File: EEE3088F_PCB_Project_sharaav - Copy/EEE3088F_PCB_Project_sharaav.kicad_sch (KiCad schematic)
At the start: 33 parts, among them Q1 NPN, Q2 PNP, Q3 NPN, Q4 PNP, SW1 SW_SPDT_MSM, U1 TPS61200DRC, U2 TPS61200DRC, U3 INA219AxDCN

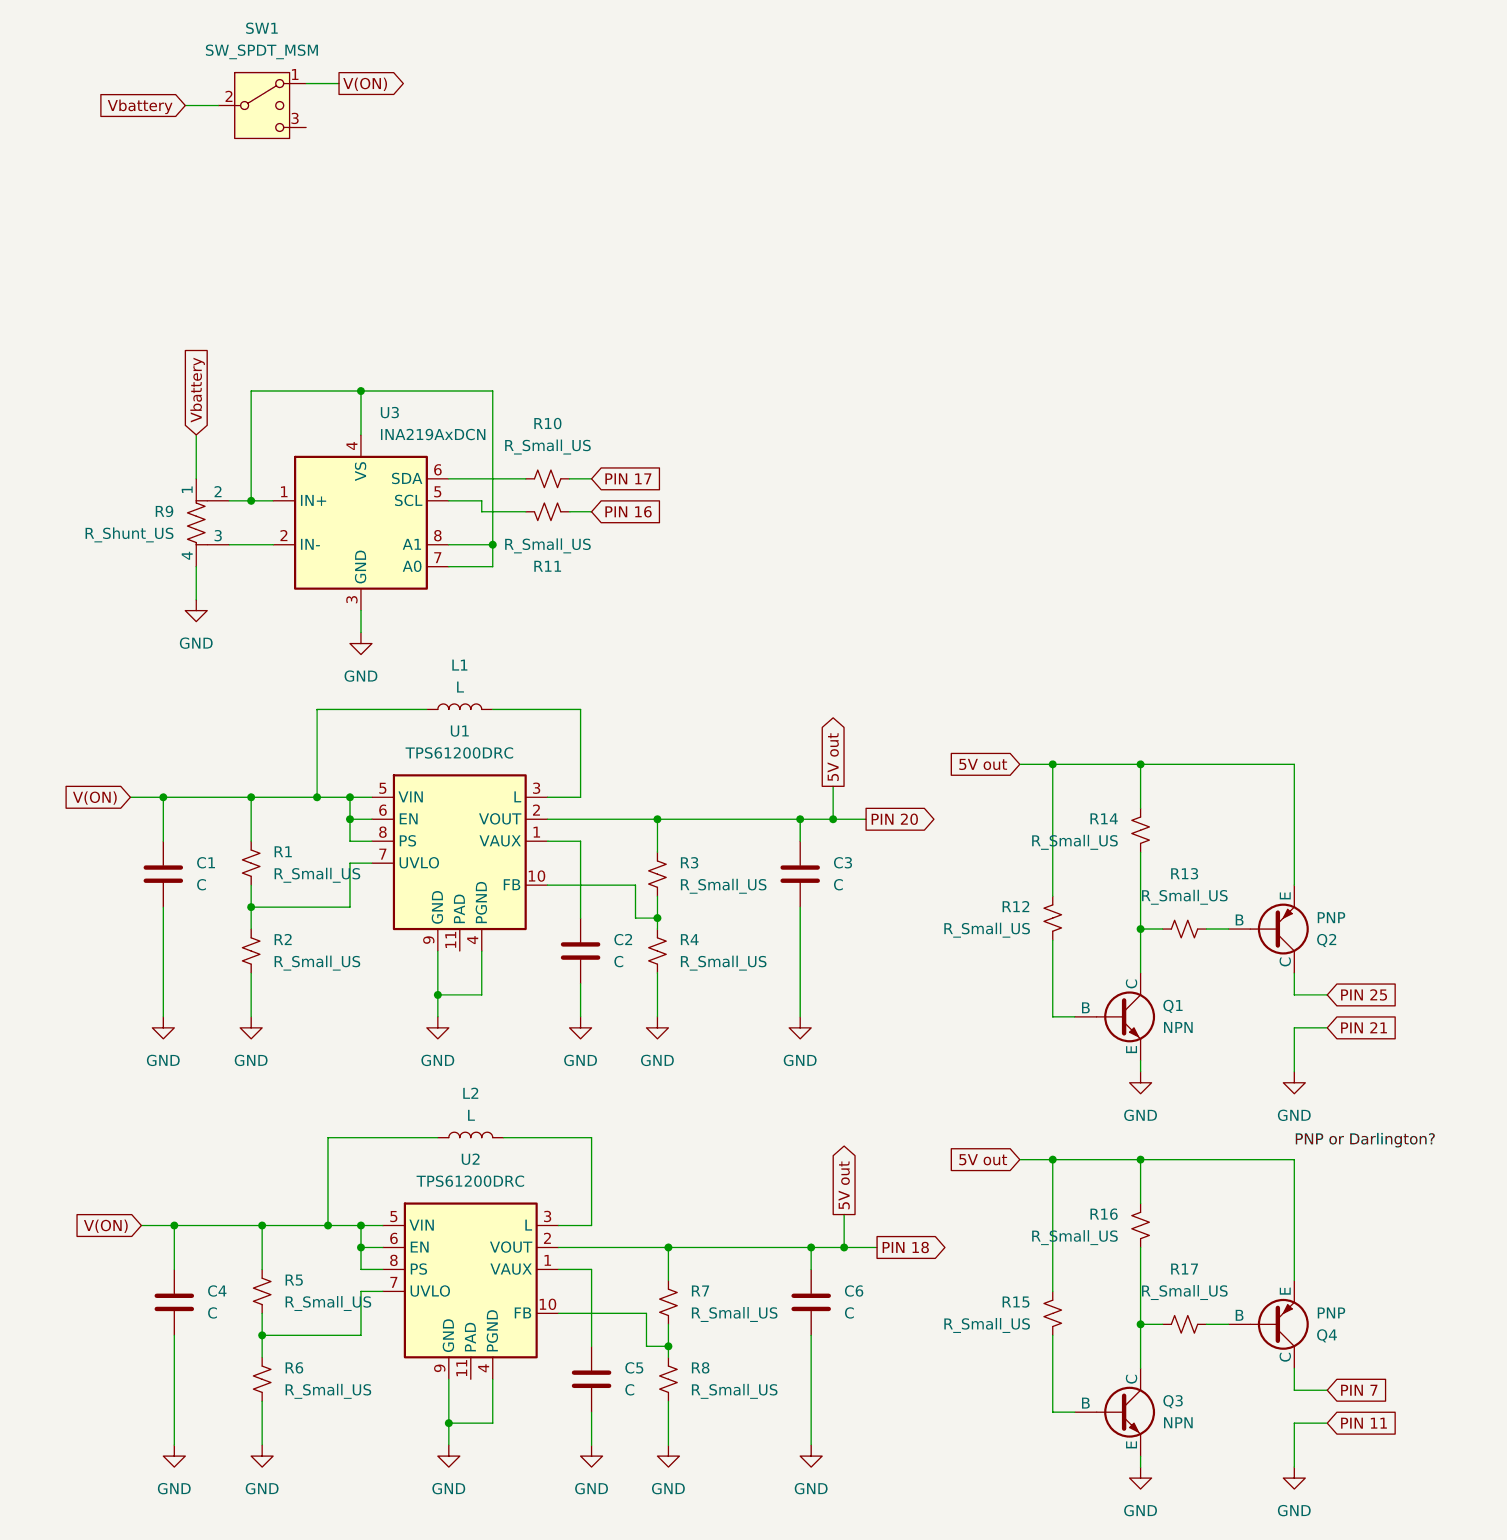
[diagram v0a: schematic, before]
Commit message: Labelled the values for passive components & added the footprints for the ICs and switch.
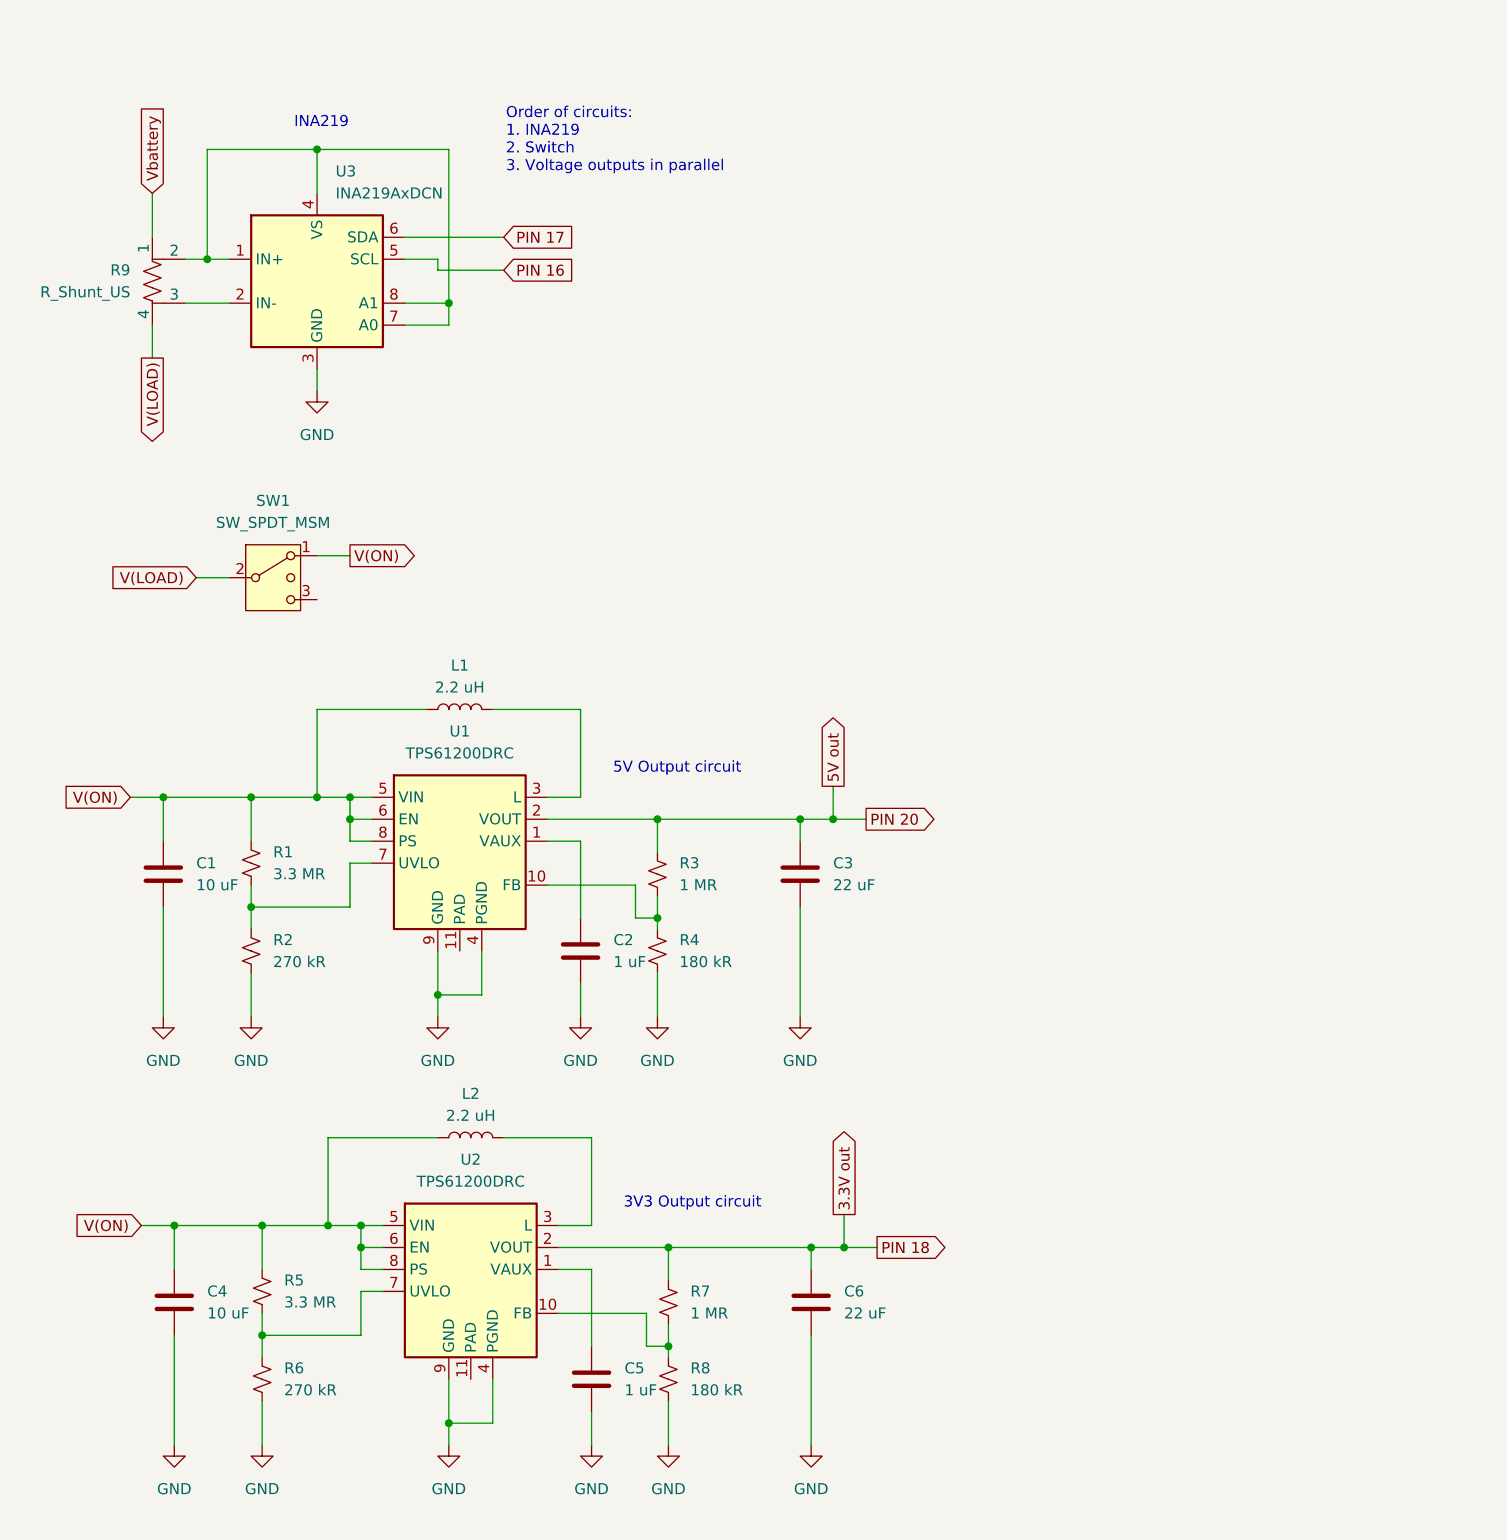
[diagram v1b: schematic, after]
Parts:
- removed Q1, Q3: NPN, symbol Simulation_SPICE:NPN
- removed Q2, Q4: PNP, symbol Simulation_SPICE:PNP
- removed R10, R11, R12, R13, R14, R15, R16, R17: R_Small_US, symbol Device:R_Small_US
- C1, C4: value C -> 10 uF
- C2, C5: value C -> 1 uF
- C3, C6: value C -> 22 uF
- L1, L2: value L -> 2.2 uH
- R1, R5: value R_Small_US -> 3.3 MR
- R2, R6: value R_Small_US -> 270 kR
- R3, R7: value R_Small_US -> 1 MR
- R4, R8: value R_Small_US -> 180 kR
- SW1: footprint (none) -> LIB_SS-12D11G5R:SS12D11G5R
- U1, U2: footprint Package_SON:Texas_S-PVSON-N10_ThermalVias -> LIB_TPS61200DRCR:TPS61200DRCR; JLCPCB Part # (none) -> C140320
- U3: footprint Package_TO_SOT_SMD:SOT-23-8 -> LIB_INA219AIDCNR:SOP65P280X145-8N
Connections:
- net 5V out: no longer C6.1, R7.1, U2.2 (VOUT)
- net GND: no longer R9.4
- net PIN 16: now also U3.5 (SCL)
- net PIN 17: now also U3.6 (SDA)
- net Vbattery: no longer SW1.2 (3)
- new net 3.3V out: C6.1, R7.1, U2.2 (VOUT)
- new net V(LOAD): R9.4, SW1.2 (3)
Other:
- note added: "3V3 Output circuit"
- note added: "5V Output circuit"
- note added: "INA219"
- note added: "Order of circuits: 1. INA219 2. Switch 3. Voltage outputs in parallel"
- moved on the sheet: R9, SW1, U3
